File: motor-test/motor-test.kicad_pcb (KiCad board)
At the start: 2 copper layers, 44 x 30 mm, 34 parts, among them J1 Conn_01x06_Male, J2 Conn_01x02_Male, J3 Conn_01x02_Male, Q1 MMBT3904, SW1 SW_DIP_x08, U2 TBD62783AFNGEL, U3 TBD62083AFNGEL, U4 X7WBX

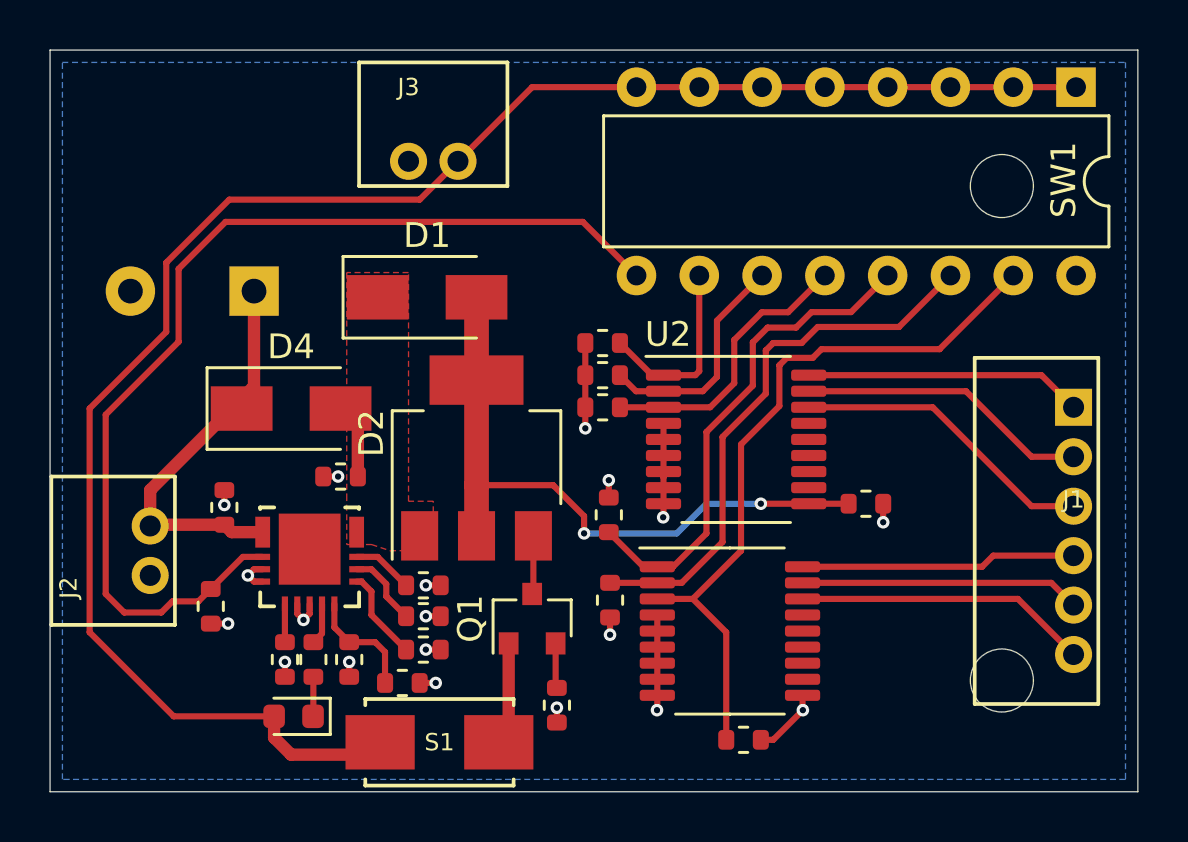
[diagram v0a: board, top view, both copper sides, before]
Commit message: design review changes fix VCC and GND swap on high side driver simplify catch diode setup to 1 diode schematic cleanup correct dV/dt cap value to give 2 ms soft start increase triac trigger current to 4.3 mA add manufacturer part numbers and data sheet link on some parts
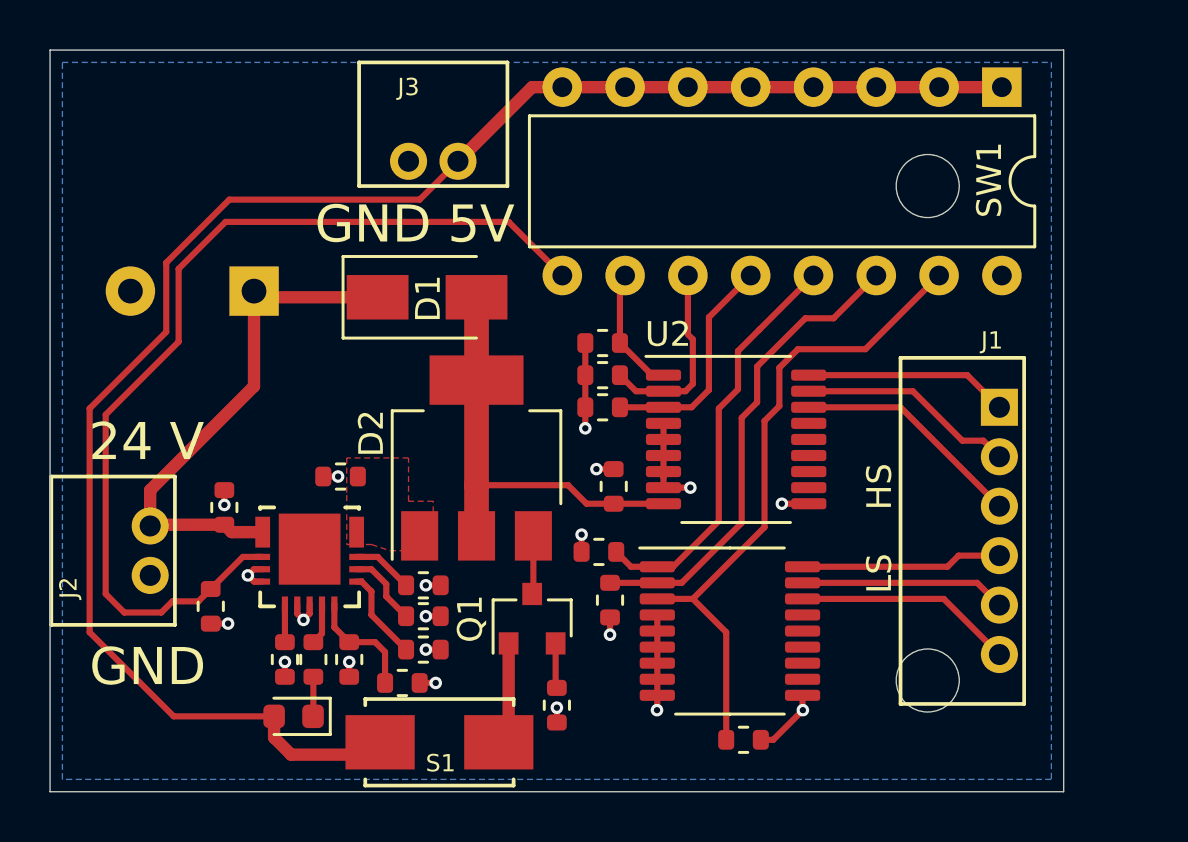
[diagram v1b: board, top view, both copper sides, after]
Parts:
- removed D4: S1GTR, Diode_SMD:D_SMA
- C6: value 100 nF -> 1 nF
- D2: value Q_TRIAC_A1A2G -> Z0103MN0
- J1: value Conn_01x06_Male -> DF3_6
- J2, J3: value Conn_01x02_Male -> DF3_2
- R1: value 2.2 k -> 1 k
- S1: value TTWY4 -> 147873-1
- SW1: value SW_DIP_x08 -> 208-8
- U4: value X7WBX -> DPS1133FIA-13
- moved C2 10.2 mm to (167.3, 72.2), turned to 90 degrees
- moved J1 3.00 mm to (182.9, 74.0)
- moved SW1 3.00 mm to (183.0, 56.0)
- moved TH1 3.00 mm to (180.0, 80.0)
- moved TH2 3.00 mm to (180.0, 60.0)
- moved R10 1.55 mm to (166.7, 74.8), turned to 0 degrees
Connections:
- D1 pad 1: /CB_OUT -> +24V
- U2 pad 10: /TRIAC_OUT -> GND
- U2 pad 9: GND -> /TRIAC_OUT
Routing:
- net /TRIAC_OUT: track 26.4 -> 17.5 mm, vias 2 -> 0
- net +24V: track 15.9 -> 21.0 mm
- net /LS0: track 20.2 -> 16.7 mm
- net /LS1: track 22.4 -> 19.3 mm
- net /LS2: track 29.6 -> 26.5 mm
- net /CB_OUT: track 3.04 -> 0.00 mm
- net Net-(J1-Pad2): track 11.8 -> 8.81 mm
- net Net-(J1-Pad6): track 11.9 -> 8.89 mm
- net Net-(J1-Pad5): track 11.3 -> 8.34 mm
- net Net-(J1-Pad3): track 12.4 -> 9.37 mm
- net Net-(J1-Pad1): track 11.3 -> 8.25 mm
- net /CB_EN: track 42.2 -> 39.2 mm
- net Net-(J1-Pad4): track 11.1 -> 8.15 mm
- net +5V: track 70.5 -> 67.5 mm
- net /HS0: track 7.68 -> 5.12 mm
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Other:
- board size 44 x 30 mm -> 41 x 30 mm
- board text added: "24 V"
- board text added: "GND"
- board text added: "GND 5V"
- board text added: "LS HS"

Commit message: change component values to available ones
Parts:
- C2: value 100 nF -> 10 nF
- R10, R11, R12, R7, R8, R9: value 5.1 k -> DNP
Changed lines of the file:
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@@
       (effects (font (size 1 1) (thickness 0.15)))
     )
-    (fp_text value "5.1 k" (at 0 1.22) (layer F.Fab)
+    (fp_text value DNP (at 0 1.22) (layer F.Fab)
       (effects (font (size 1 1) (thickness 0.15)))
     )
@@
       (effects (font (size 1 1) (thickness 0.15)))
     )
-    (fp_text value "5.1 k" (at 0 1.22 90) (layer F.Fab)
+    (fp_text value DNP (at 0 1.22 90) (layer F.Fab)
       (effects (font (size 1 1) (thickness 0.15)))
     )
@@
       (effects (font (size 1 1) (thickness 0.15)))
     )
-    (fp_text value "5.1 k" (at 0 1.22) (layer F.Fab)
+    (fp_text value DNP (at 0 1.22) (layer F.Fab)
       (effects (font (size 1 1) (thickness 0.15)))
     )
@@
       (effects (font (size 1 1) (thickness 0.15)))
     )
-    (fp_text value "5.1 k" (at 0 1.22) (layer F.Fab)
+    (fp_text value DNP (at 0 1.22) (layer F.Fab)
       (effects (font (size 1 1) (thickness 0.15)))
     )
@@
       (effects (font (size 1 1) (thickness 0.15)))
     )
-    (fp_text value "5.1 k" (at 0 1.22) (layer F.Fab)
+    (fp_text value DNP (at 0 1.22) (layer F.Fab)
       (effects (font (size 1 1) (thickness 0.15)))
     )
@@
       (effects (font (size 1 1) (thickness 0.15)))
     )
-    (fp_text value "5.1 k" (at 0 1.22) (layer F.Fab)
+    (fp_text value DNP (at 0 1.22) (layer F.Fab)
       (effects (font (size 1 1) (thickness 0.15)))
     )
@@
       (effects (font (size 1 1) (thickness 0.15)))
     )
-    (fp_text value "100 nF" (at 0 1.22 90) (layer F.Fab)
-      (effects (font (size 1 1) (thickness 0.15)))
-    )
+    (fp_text value "10 nF" (at 0 1.22 90) (layer F.Fab)
+      (effects (font (size 1 1) (thickness 0.15)))
+    )
